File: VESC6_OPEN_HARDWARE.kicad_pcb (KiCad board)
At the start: 2 copper layers, 112.6 x 46.7 mm, 125 parts, among them P1 USB_OTG, P10 PH_A, P11 SUPPLY, P12 GND, P2 TS_CAN, P3 SWD, P4 HALL/Encoder, P5 TS_CAN, P7 Custom, P8 PH_C, P9 PH_B, Q1 STL130N6F7, Q2 STL130N6F7, Q3 STL130N6F7, Q4 STL130N6F7, Q5 STL130N6F7, Q6 STL130N6F7, U1 STM32F40X_LQFP64, U10 LSM6DS3TR-C, U2 LM3671, U3 DRV8301, U4 TJA1051TK-3, U5 AD8418, U6 AD8418, U7 AD8418, X1 8m

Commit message: Adjusted connectors and routing
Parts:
- P3: footprint Connector_PinSocket_1.27mm:PinSocket_1x06_P1.27mm_Vertical -> Connector_JST:JST_SH_SM06B-SRSS-TB_1x06-1MP_P1.00mm_Horizontal
- moved P3 51.5 mm to (57.9, 3.63), turned to 180 degrees
- moved C36 44.1 mm to (17.4, 39.7)
- moved R27 44.1 mm to (19.7, 40.5)
- moved R28 44.1 mm to (17.4, 41.3)
- moved C12 42.3 mm to (93.6, 14.3)
- moved C14 42.3 mm to (71.0, 19.7)
- moved C16 42.3 mm to (62.5, 33.4)
- moved C18 42.3 mm to (62.9, 27.2)
- moved C21 42.3 mm to (72.3, 33.2)
- moved C24 42.3 mm to (52.1, 18.9)
- moved C25 42.3 mm to (52.1, 16.2)
- moved C26 42.3 mm to (52.0, 12.6)
- moved C29 42.3 mm to (35.4, 31.3)
- moved C31 42.3 mm to (59.1, 37.7)
- moved C4 42.3 mm to (76.0, 12.8)
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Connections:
- P3 pad 1: VCC -> +5V
- P3 pad 2: /stm32f40x/SWCLK -> /stm32f40x/NRST
- P3 pad 3: GND -> /stm32f40x/SWDIO
- P3 pad 4: /stm32f40x/SWDIO -> GND
- P3 pad 5: /stm32f40x/NRST -> /stm32f40x/SWCLK
- P3 pad 6: unconnected-(P3-Pin_6-Pad6) -> VCC
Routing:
- net /stm32f40x/NRST: track 11.0 -> 69.8 mm, vias 0 -> 2
- net /stm32f40x/SWCLK: track 2.06 -> 31.8 mm, vias 1 -> 4
- net +5V: track 182.0 -> 209.2 mm, vias 5 -> 7
- net /stm32f40x/SWDIO: track 5.78 -> 27.7 mm, vias 1 -> 2
- net /stm32f40x/PB12: track 0.00 -> 9.98 mm
- net VCC: track 270.5 -> 277.6 mm, vias 10 -> 11
- net /stm32f40x/USB_DM: track 19.4 -> 12.6 mm
- net /stm32f40x/USB_DP: track 21.0 -> 15.0 mm
- net /DRV8301/CS: track 40.9 -> 42.7 mm
- net /power/TEMP: track 84.2 -> 85.1 mm
- net Net-(P1-VBUS): track 3.66 -> 2.93 mm
- net /DRV8301/SENS_A: track 52.3 -> 52.9 mm
- net GND: vias 85 -> 96
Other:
- board size 112.6 x 46.7 mm -> 112 x 47 mm
- board text added: "ADC port EN_BUCK switch"
- board text removed: "ADC port Aditional CAN port for BMS"

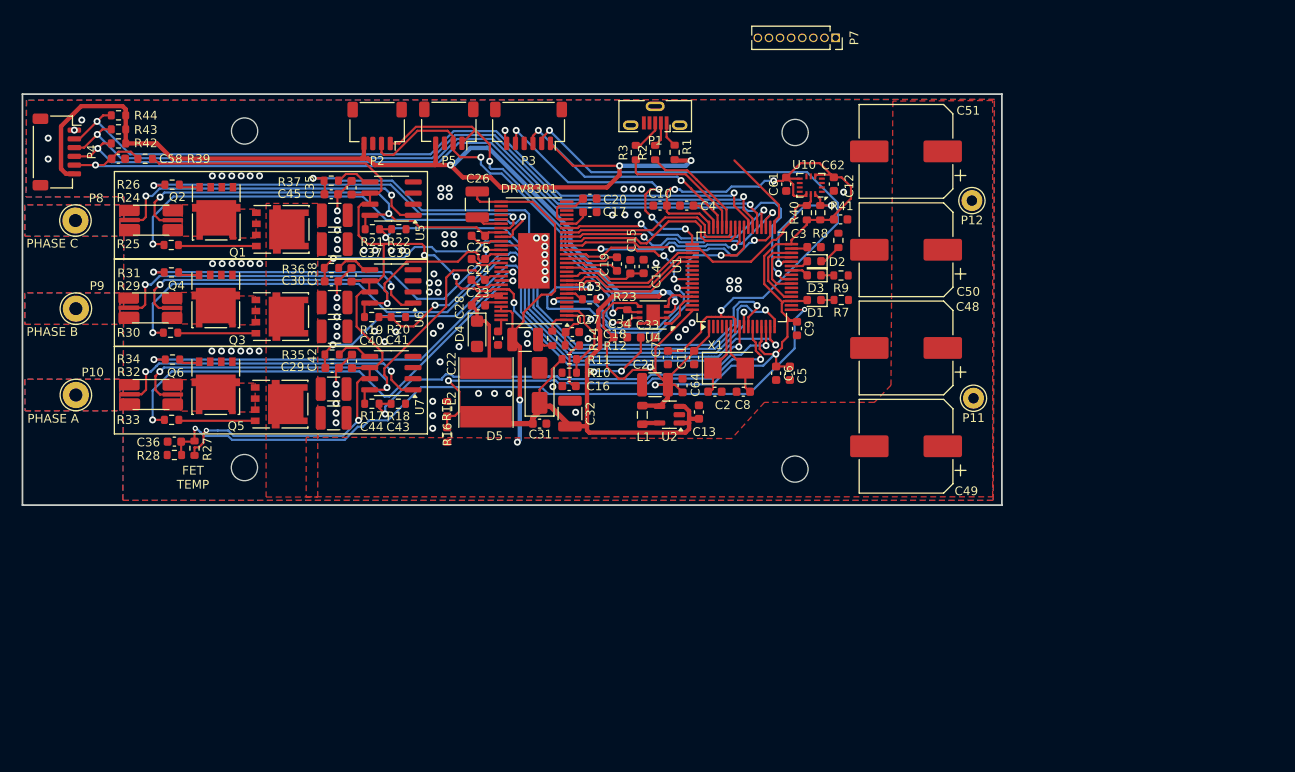
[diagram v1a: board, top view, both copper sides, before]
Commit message: Board resized and changed usb port
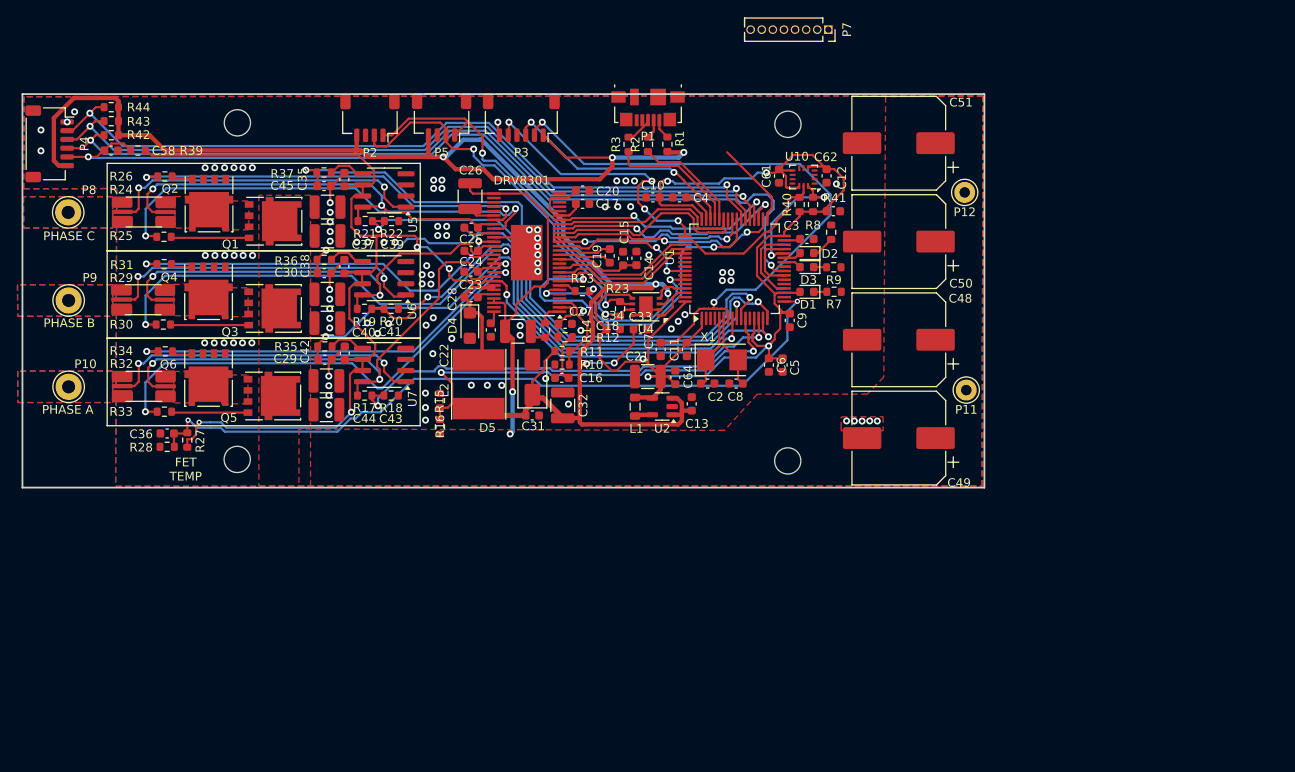
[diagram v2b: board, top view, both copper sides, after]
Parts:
- P1: footprint Connector_USB:USB_Micro-B_Molex-105133-0001 -> Connector_USB:USB_Micro-B_Molex_47346-0001
- moved C11 1.25 mm to (76.0, 29.2)
- moved C13 1.25 mm to (76.5, 35.4)
- moved C14 1.25 mm to (70.2, 18.8)
- moved C18 1.25 mm to (62.1, 26.3)
- moved C31 1.25 mm to (58.3, 36.8)
- moved C33 1.25 mm to (70.7, 26.9)
- moved C43 1.25 mm to (34.8, 36.1)
- moved C44 1.25 mm to (34.8, 32.8)
- moved C48 1.25 mm to (100.2, 28.1)
- moved C49 1.25 mm to (100.2, 39.3)
- moved C50 1.25 mm to (100.2, 16.9)
- moved C6 1.25 mm to (85.4, 31.0)
- moved C64 1.25 mm to (74.7, 32.4)
- moved C7 1.25 mm to (73.0, 29.2)
- moved D1 1.25 mm to (89.7, 22.6)
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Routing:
- net GND: vias 96 -> 101
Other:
- board size 112 x 47 mm -> 110 x 45 mm

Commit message: changed connectors, needs final routing and drc
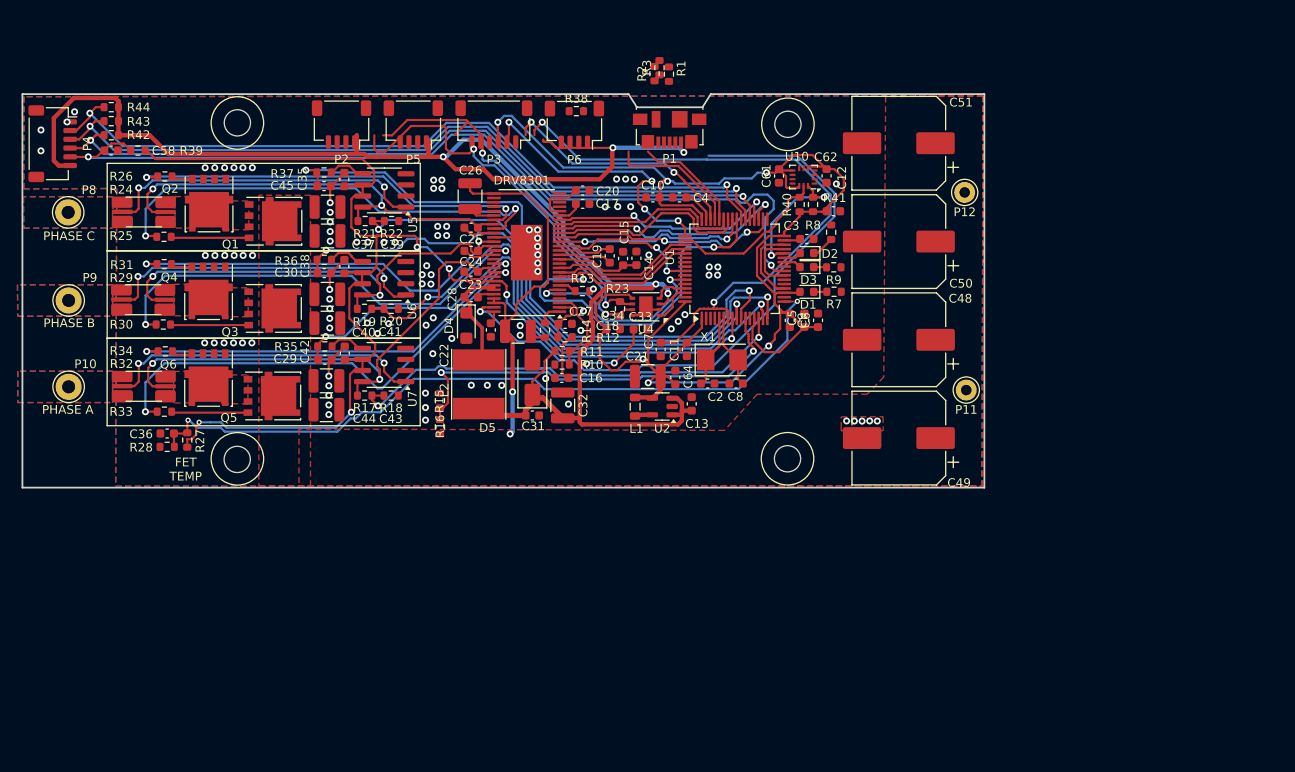
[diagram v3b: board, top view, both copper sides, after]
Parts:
- removed P7: Custom, Connector_PinSocket_1.27mm:PinSocket_1x08_P1.27mm_Vertical
- added P6: TS_CAN, Connector_JST:JST_SH_SM04B-SRSS-TB_1x04-1MP_P1.00mm_Horizontal, F.Cu at (63.1, 3.52)
- added R38: 10k, Resistor_SMD:R_0603_1608Metric, F.Cu at (63.3, 1.95)
- moved R3 9.45 mm to (72.8, -3.02)
- moved R2 8.12 mm to (72.3, -2.33)
- moved R1 8.02 mm to (73.9, -2.28)
- moved C6 7.60 mm to (91.0, 25.9), turned to 90 degrees
- moved C5 5.69 mm to (89.4, 25.9), turned to 90 degrees
- moved P1 3.55 mm to (74.0, 4.08)
- moved P2 3.34 mm to (36.5, 3.48)
- moved P5 3.33 mm to (44.7, 3.48)
- moved P3 3.24 mm to (53.9, 3.48)
- moved D4 0.40 mm to (50.8, 26.5)
- moved P4 0.35 mm to (3.46, 5.67)
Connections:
- U3 pad 55: unconnected-(U3-EN_BUCK-Pad55) -> /DRV8301/SWITCH-
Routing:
- net /DRV8301/SWITCH-: track 0.00 -> 73.2 mm, vias 0 -> 1
- net VCC: track 277.6 -> 307.5 mm
- net /stm32f40x/PB12: track 9.98 -> 0.00 mm
- net Net-(P1-D+): track 3.77 -> 0.00 mm
- net Net-(P1-VBUS): track 2.93 -> 0.00 mm
- net Net-(P1-D-): track 2.84 -> 0.00 mm
- net +5V: track 209.2 -> 207.1 mm
- net /CAN/CANH: track 45.2 -> 46.5 mm
- net /DRV8301/SENS_C: track 61.5 -> 62.3 mm
- net /power/CURR_C: track 73.4 -> 74.1 mm
- net Net-(D4-K): track 13.2 -> 12.6 mm
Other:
- outline, holes or cut-outs redrawn

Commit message: Finished routing
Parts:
- P2: value TS_CAN -> CAN2
- P5: value TS_CAN -> CAN1
- P6: value TS_CAN -> ADC_SWITCH
- moved R2 13.5 mm to (78.9, 9.47)
- moved R3 13.3 mm to (77.3, 9.47)
- moved R1 11.2 mm to (69.8, 8.15), turned to 0 degrees
- moved R38 5.55 mm to (68.1, 4.80), turned to 90 degrees
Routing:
- net /stm32f40x/SCK_ADC_EXT: track 0.00 -> 48.2 mm, vias 0 -> 2
- net Net-(P1-VBUS): track 0.00 -> 18.2 mm, vias 0 -> 2
- net /DRV8301/SWITCH-: track 73.2 -> 89.6 mm, vias 1 -> 2
- net +5V: track 207.1 -> 196.3 mm, vias 7 -> 5
- net /stm32f40x/USB_DP: track 15.0 -> 4.77 mm
- net GND: track 25.8 -> 34.1 mm, vias 101 -> 132
- net /stm32f40x/USB_DM: track 12.6 -> 4.33 mm
- net Net-(P1-D-): track 0.00 -> 6.07 mm
- net /stm32f40x/NRST: track 69.8 -> 75.6 mm
- net /stm32f40x/SWDIO: track 27.7 -> 33.2 mm
- net Net-(P1-D+): track 0.00 -> 5.16 mm
- net /stm32f40x/SWCLK: track 31.8 -> 35.3 mm
- net VCC: track 307.5 -> 310.5 mm
- net /CAN/CANL: track 44.4 -> 46.2 mm, vias 2 -> 4
- net /CAN/CANH: track 46.5 -> 48.2 mm
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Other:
- board text added: "TODO Mounting holes as footprints with exact positions Phase and battery footprints with exact positions DRC Review ground routing"
- board text removed: "ADC port EN_BUCK switch"

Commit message: Finished traces, DRC Passed, Grounding needs revised
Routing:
- net /stm32f40x/TEMP_MOTOR: track 101.1 -> 104.3 mm
- net GND: track 34.1 -> 31.1 mm, vias 132 -> 144
- net /stm32f40x/SWCLK: track 35.3 -> 32.7 mm
- net /DRV8301/GL_A: track 48.0 -> 50.4 mm
- net /DRV8301/SH_A: track 59.2 -> 58.2 mm
- net /DRV8301/GH_A: track 54.9 -> 53.9 mm
- net /IMU/SDA: track 15.3 -> 14.4 mm
- net VCC: track 310.5 -> 309.7 mm
- net Net-(D2-K): track 2.63 -> 3.24 mm
- removed copper zone on B.Cu, net Net-(P10-Pin_1)
- removed copper zone on B.Cu, net Net-(P8-Pin_1)
- removed copper zone on B.Cu, net Net-(P9-Pin_1)
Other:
- board text added: "TODO Mounting holes as footprints with exact positions Phase and battery footprints with exact positions DRC Review ground routing double check single spoke gnd releifs"
- board text removed: "TODO Mounting holes as footprints with exact positions Phase and battery footprints with exact positions DRC Review ground routing"

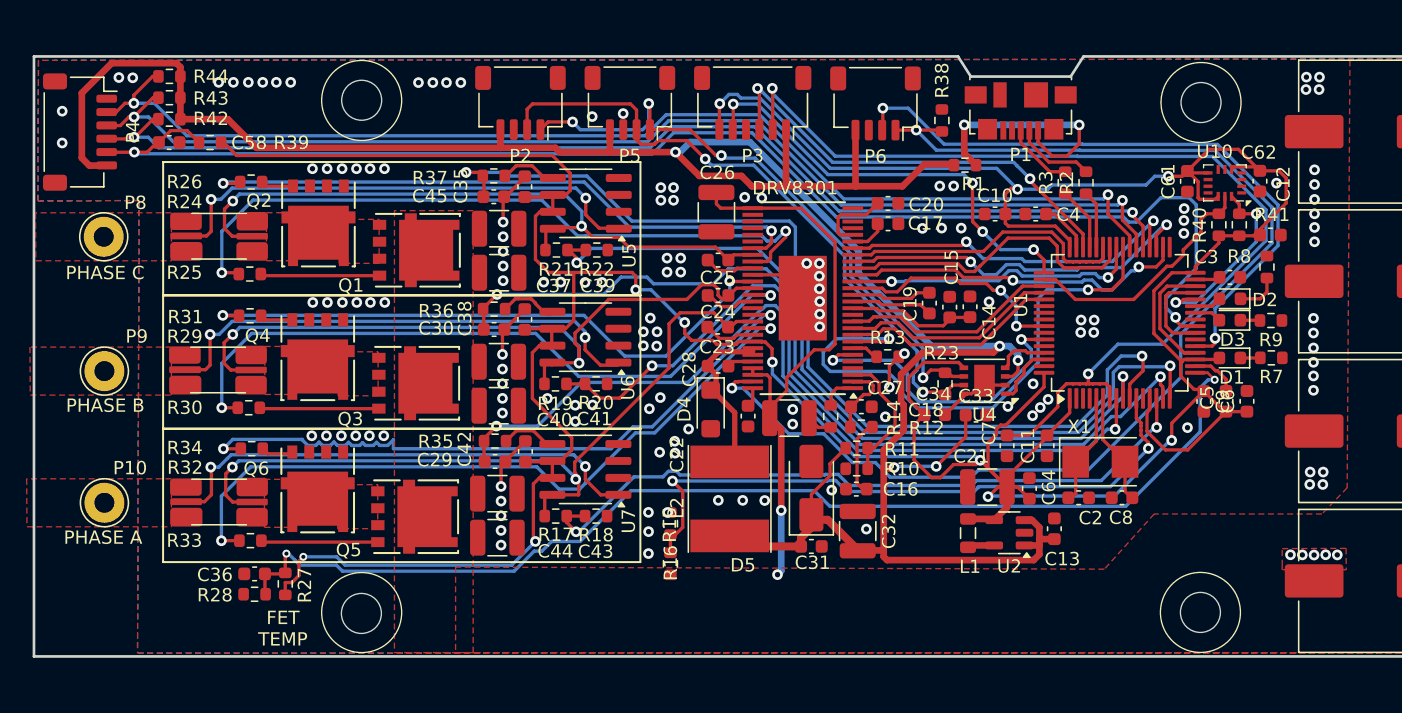
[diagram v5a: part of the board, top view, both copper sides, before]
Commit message: mounting holes, more grounding and routing
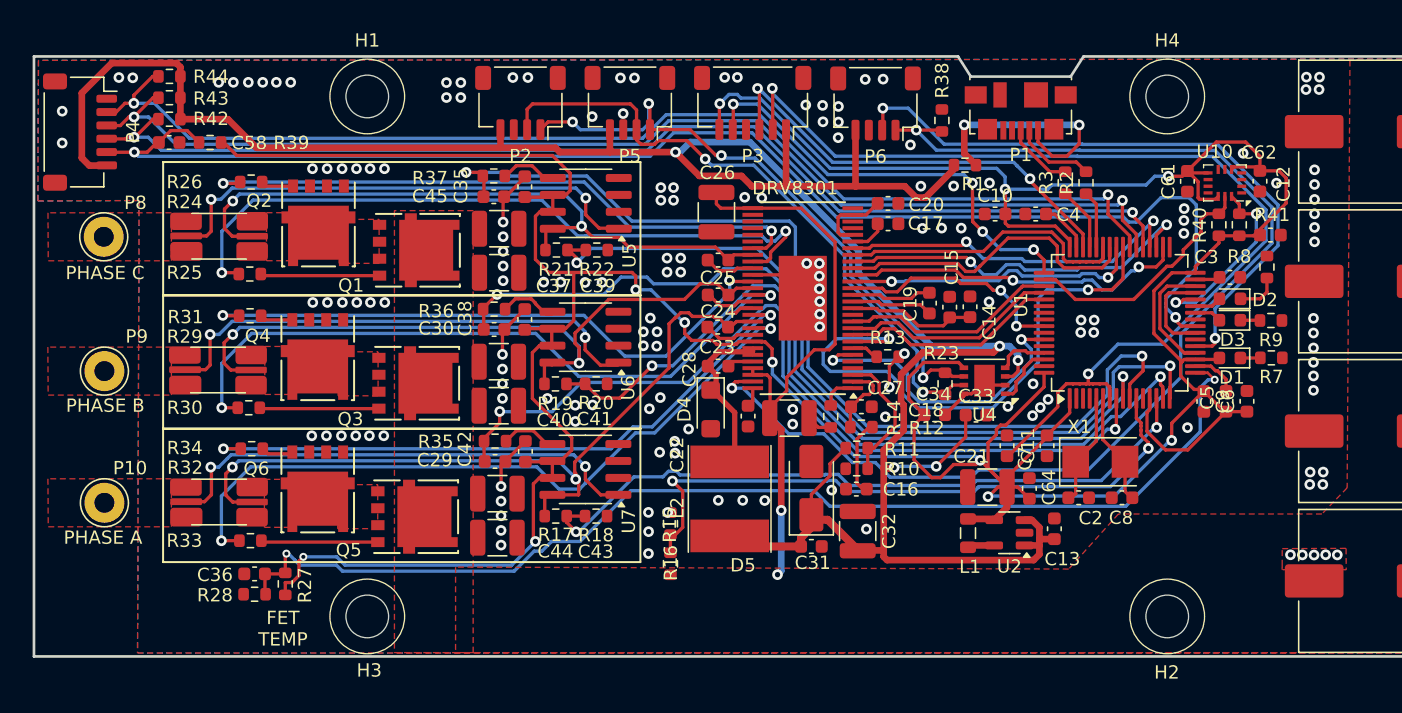
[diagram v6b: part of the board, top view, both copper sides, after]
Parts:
- added H1: MountingHole, CustomFootprints:MountingHole_3mm, F.Cu at (25.0, 3.00)
- added H2: MountingHole, CustomFootprints:MountingHole_3mm, F.Cu at (85.0, 42.0)
- added H3: MountingHole, CustomFootprints:MountingHole_3mm, F.Cu at (25.0, 42.0)
- added H4: MountingHole, CustomFootprints:MountingHole_3mm, F.Cu at (85.0, 3.00)
- turned C7 to 90 degrees
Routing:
- net /DRV8301/GL_A: track 50.4 -> 48.0 mm
- net GND: track 31.1 -> 32.9 mm, vias 144 -> 160
- net +5V: track 196.3 -> 197.3 mm
- net VCC: track 309.7 -> 310.5 mm
- net /stm32f40x/NRST: track 75.6 -> 76.3 mm
- net /power/CURR_A: track 63.6 -> 64.1 mm
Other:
- outline, holes or cut-outs redrawn
- board text added: "TODO Phase and battery footprints with exact positions Probs gonna need inner layers :( grounding is not good enough"
- board text removed: "TODO Mounting holes as footprints with exact positions Phase and battery footprints with exact positions DRC Review ground routing double check single spoke gnd releifs"

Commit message: drc clear, added images
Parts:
- P11, P12: footprint Connector_Pin:Pin_D1.0mm_L10.0mm_LooseFit -> Connector_Pin:Pin_D1.3mm_L11.0mm_LooseFit
- moved P11 0.37 mm to (107.6, 33.8)
- moved P12 0.19 mm to (107.6, 11.2)
- moved P6 0.06 mm to (63.1, 3.46)
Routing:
- added copper zone on In1.Cu, net GND
- added copper zone on In2.Cu, net GND
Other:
- outline, holes or cut-outs redrawn
- copper layers 2 -> 4
- board text added: "DRV"
- board text added: "GND"
- board text added: "SUPPLY"
- board text removed: "DRV8301"
- board text removed: "TODO Phase and battery footprints with exact positions Probs gonna need inner layers :( grounding is not good enough"

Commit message: Release
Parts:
- removed D1: BLUE, Diode_SMD:D_0603_1608Metric
- removed R7: 1k, Resistor_SMD:R_0603_1608Metric
- added G***: LOGO, LOGO, F.Cu at (69.0, 41.5)
- added G***: LOGO, LOGO, F.Cu at (76.5, 41.5)
- added G***: LOGO, LOGO, F.Cu at (46.8, 41.5)
- D3: value GREEN -> WHITE
- moved R15 2.01 mm to (46.2, 36.8)
- moved P9 0.30 mm to (5.00, 23.5)
- moved P10 0.29 mm to (5.00, 33.5)
- moved P8 0.24 mm to (5.00, 13.5)
- moved P11 0.08 mm to (107.5, 33.8)
- moved P12 0.06 mm to (107.5, 11.2)
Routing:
- net VCC: track 310.5 -> 308.7 mm
- net Net-(D1-K): track 1.50 -> 0.00 mm
- net SUPPLY: track 43.1 -> 43.7 mm
- net GND: vias 160 -> 203
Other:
- board text added: "Designed by Craig Gault github.com/craigg96"
- board text removed: "FET TEMP"
